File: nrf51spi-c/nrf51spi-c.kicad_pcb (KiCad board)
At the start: 2 copper layers, 21.1 x 13.7 mm, 23 parts, among them J1 Conn_01x09, J2 Conn_01x07, U1 nRF51x22-QFxx, Y1 16MHz

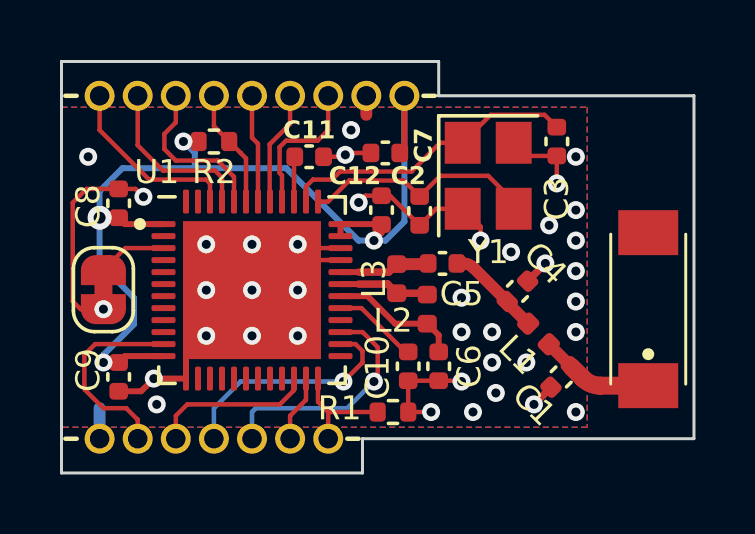
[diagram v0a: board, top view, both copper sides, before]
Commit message: Add teradrops and castellated holes
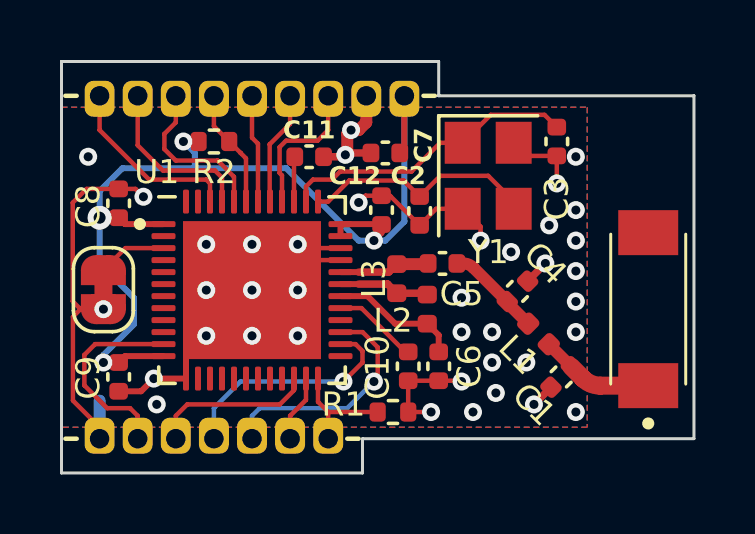
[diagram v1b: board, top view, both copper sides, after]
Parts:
- added J10: Conn_01x01_Socket, nrf51_module:castellated_holes_1.27mm, F.Cu at (134.6, 82.4)
- added J11: Conn_01x01_Socket, nrf51_module:castellated_holes_1.27mm, F.Cu at (141.0, 93.9)
- added J12: Conn_01x01_Socket, nrf51_module:castellated_holes_1.27mm, F.Cu at (139.7, 93.9)
- added J13: Conn_01x01_Socket, nrf51_module:castellated_holes_1.27mm, F.Cu at (138.4, 93.9)
- added J14: Conn_01x01_Socket, nrf51_module:castellated_holes_1.27mm, F.Cu at (137.2, 93.9)
- added J15: Conn_01x01_Socket, nrf51_module:castellated_holes_1.27mm, F.Cu at (135.9, 93.9)
- added J16: Conn_01x01_Socket, nrf51_module:castellated_holes_1.27mm, F.Cu at (134.6, 93.9)
- added J3: Conn_01x01_Socket, nrf51_module:castellated_holes_1.27mm, F.Cu at (144.8, 82.4)
- added J4: Conn_01x01_Socket, nrf51_module:castellated_holes_1.27mm, F.Cu at (142.2, 82.4)
- added J5: Conn_01x01_Socket, nrf51_module:castellated_holes_1.27mm, F.Cu at (141.0, 82.4)
- added J6: Conn_01x01_Socket, nrf51_module:castellated_holes_1.27mm, F.Cu at (139.7, 82.4)
- added J7: Conn_01x01_Socket, nrf51_module:castellated_holes_1.27mm, F.Cu at (138.4, 82.4)
- added J8: Conn_01x01_Socket, nrf51_module:castellated_holes_1.27mm, F.Cu at (137.2, 82.4)
- added J9: Conn_01x01_Socket, nrf51_module:castellated_holes_1.27mm, F.Cu at (135.9, 82.4)
- J1: value Conn_01x09 -> Conn_01x01_Socket; footprint Connector_PinHeader_1.27mm:PinHeader_1x09_P1.27mm_Vertical -> nrf51_module:castellated_holes_1.27mm; moved to F.Cu
- J2: value Conn_01x07 -> Conn_01x01_Socket; footprint Connector_PinHeader_1.27mm:PinHeader_1x07_P1.27mm_Vertical -> nrf51_module:castellated_holes_1.27mm; moved to F.Cu
- moved J1 1.27 mm to (143.5, 82.4), turned to -90 degrees
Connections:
- J1 pad 1: VDD -> GND
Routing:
- net GND: track 36.9 -> 43.6 mm
